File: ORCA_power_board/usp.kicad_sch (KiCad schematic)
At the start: 52 parts, among them J21 Conn_01x02, Q5 TJ60S04M3L, U10 HY2112, U11 AP64502, U12 TPS61230A__board, U3 CN3058E, U9 FS8205

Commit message: fixed most of the error. waiting check
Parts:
- U3: footprint Package_SO:TSSOP-8_3x3mm_P0.65mm -> Package_SO:HTSOP-8-1EP_3.9x4.9mm_P1.27mm_EP2.4x3.2mm
- U9: value FS8205 -> FS8205A; footprint Package_TO_SOT_SMD:TSOT-23-6_HandSoldering -> Package_SO:TSSOP-8_4.4x3mm_P0.65mm
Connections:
- net +VDD_usp: now also R33.1; no longer R33.2
- net GND: now also U3.9 (GND), U9.2
- net batt+: now also Q5.3 (S); no longer Q5.1 (D)
- net batt-: now also U9.6, U9.7; no longer U9.1
- net reg_up: now also Q5.1 (D); no longer Q5.3 (S)
- net at U10.1 (OD): now also U9.5; no longer U9.6
- net at Q5.2 (G): now also R33.2; no longer R33.1
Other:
- moved on the sheet: D15, D17, Q5, R31, R32, R33

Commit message: complete power_board
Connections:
- net +VDD_usp: now also R33.2; no longer R33.1
- net at Q5.2 (G): now also R33.1; no longer R33.2
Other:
- moved on the sheet: C24, C25, C26, C27, C28, C29, C30, C31, C32, C33, C34, C35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

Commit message: ordered power board
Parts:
- U10: footprint Package_TO_SOT_SMD:TSOT-23-6_HandSoldering -> Package_TO_SOT_SMD:TSOT-23-6
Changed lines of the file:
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@@
 			)
 		)
-		(property "Footprint" "Package_TO_SOT_SMD:TSOT-23-6_HandSoldering"
+		(property "Footprint" "Package_TO_SOT_SMD:TSOT-23-6"
 			(at 224.79 86.36 0)
 			(effects

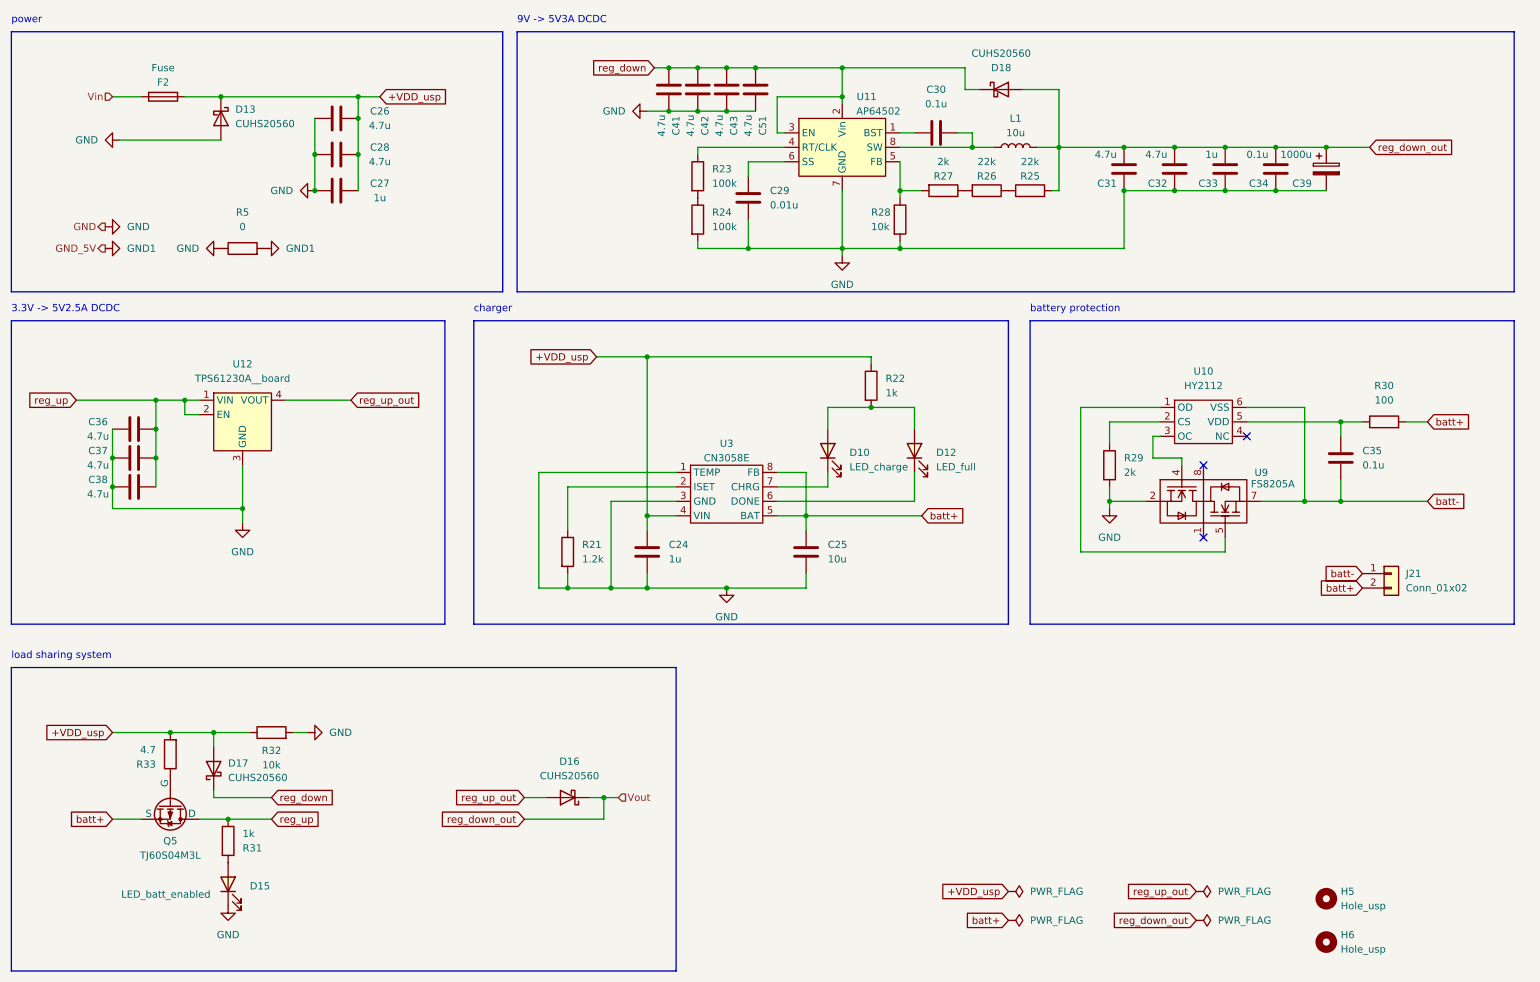
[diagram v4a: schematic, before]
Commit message: correct few errors in usp
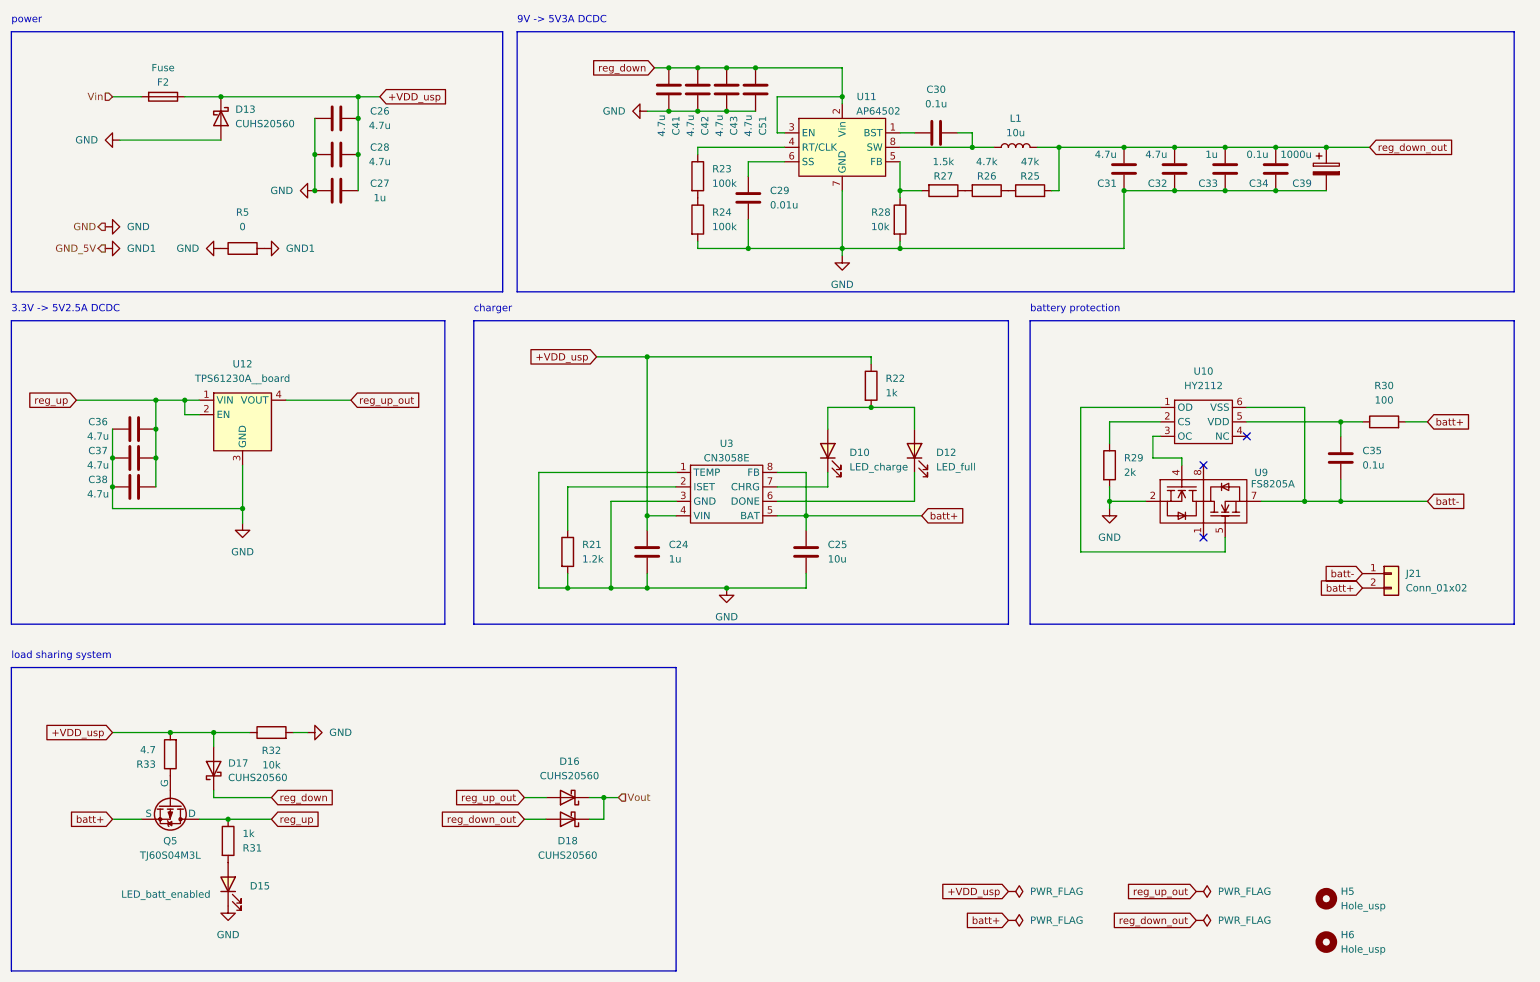
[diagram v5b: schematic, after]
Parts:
- R25: value 22k -> 47k
- R26: value 22k -> 4.7k
- R27: value 2k -> 1.5k
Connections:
- net reg_down: no longer D18.1 (K)
- net reg_down_out: no longer D16.1 (K)
- new net Vout: D16.1 (K), D18.1 (K)
